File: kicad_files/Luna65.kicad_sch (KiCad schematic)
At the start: 384 parts, among them J1 Molex Power, J2 uC Pin Headers, J3 nRF51 Pin Headers, SW0 SW_Push, SW1 Mechanical_Switch, SW10 Mechanical_Switch, SW11 Mechanical_Switch, SW12 Mechanical_Switch, SW13 Mechanical_Switch, SW14 Mechanical_Switch, SW15 Mechanical_Switch, SW16 Mechanical_Switch, SW17 Mechanical_Switch, SW18 Mechanical_Switch, SW19 Mechanical_Switch, SW2 Mechanical_Switch, SW20 Mechanical_Switch, SW21 Mechanical_Switch, SW22 Mechanical_Switch, SW23 Mechanical_Switch, SW24 Mechanical_Switch, SW25 Mechanical_Switch, SW26 Mechanical_Switch, SW27 Mechanical_Switch, SW28 Mechanical_Switch, SW29 Mechanical_Switch, SW3 Mechanical_Switch, SW30 Mechanical_Switch, SW31 Mechanical_Switch, SW32 Mechanical_Switch, SW33 Mechanical_Switch, SW34 Mechanical_Switch, SW35 Mechanical_Switch, SW36 Mechanical_Switch, SW37 Mechanical_Switch, SW38 Mechanical_Switch, SW39 Mechanical_Switch, SW4 Mechanical_Switch, SW40 Mechanical_Switch, SW41 Mechanical_Switch, SW42 Mechanical_Switch, SW43 Mechanical_Switch, SW44 Mechanical_Switch, SW45 Mechanical_Switch, SW46 Mechanical_Switch, SW47 Mechanical_Switch, SW48 Mechanical_Switch, SW49 Mechanical_Switch, SW5 Mechanical_Switch, SW50 Mechanical_Switch, SW51 Mechanical_Switch, SW52 Mechanical_Switch, SW53 Mechanical_Switch, SW54 Mechanical_Switch, SW55 Mechanical_Switch, SW56 Mechanical_Switch, SW57 Mechanical_Switch, SW58 Mechanical_Switch, SW59 Mechanical_Switch, SW6 Mechanical_Switch, SW60 Mechanical_Switch, SW61 Mechanical_Switch, SW62 Mechanical_Switch, SW63 Mechanical_Switch, SW64 Mechanical_Switch, SW65 Mechanical_Switch, SW66 Mechanical_Switch, SW67 Mechanical_Switch, SW68 Mechanical_Switch, SW7 Mechanical_Switch, SW8 Mechanical_Switch, SW9 Mechanical_Switch, U1 ATMEGA32U4, U2 MBT40, U3 TXS0101DBVR, Y1 16MHz

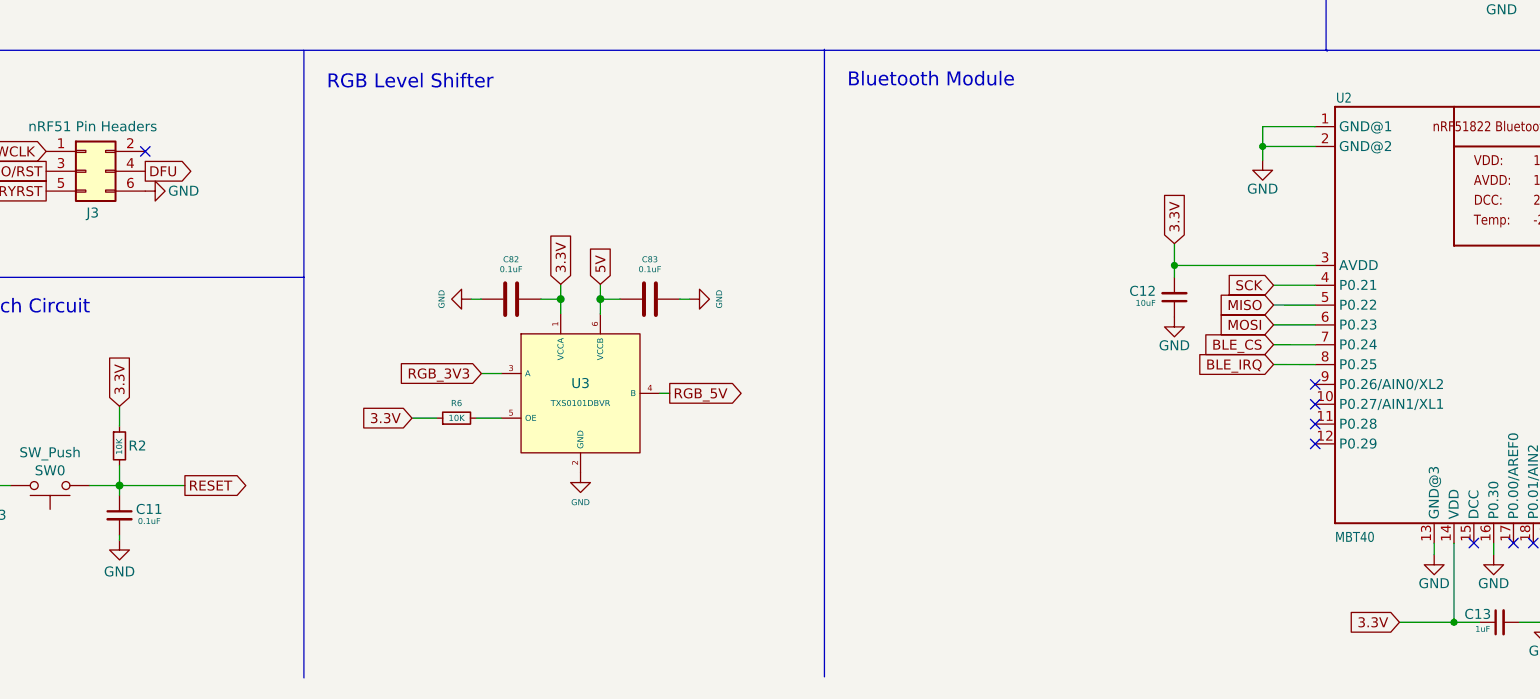
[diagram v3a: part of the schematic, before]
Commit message: Added 0 Ohm resistor to isolate BT and uC 3.3V
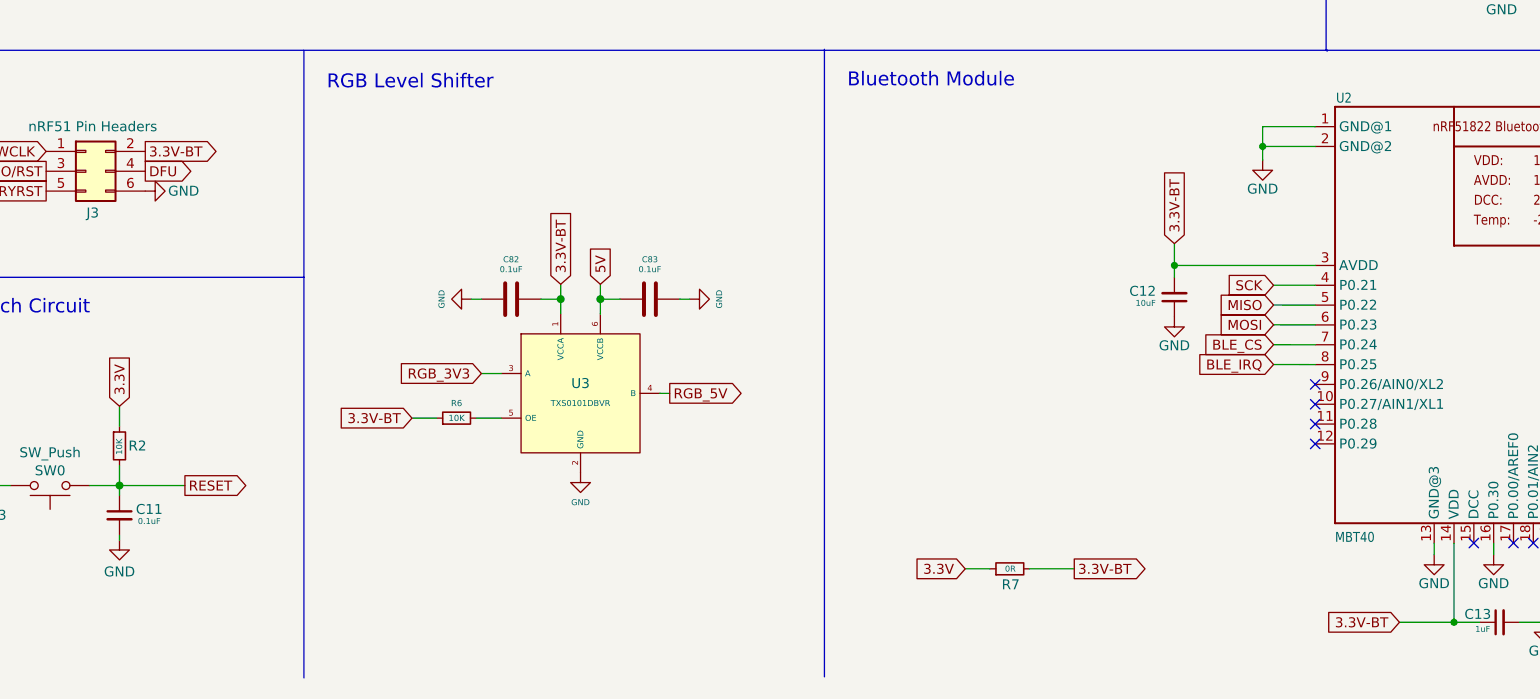
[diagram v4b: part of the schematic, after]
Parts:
- added R7: 0R, acheron_Components:R_SMD_1206, symbol Device:R_Small
- R6: footprint Resistor_SMD:R_0805_2012Metric_Pad1.20x1.40mm_HandSolder -> acheron_Components:C_0805_2012Metric
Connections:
- net 3.3V: now also R7.1; no longer C12.2, C13.1, C82.2, R6.1, U2.14 (VDD), U2.3 (AVDD), U3.1 (VCCA)
- net 3.3V-BT: now reaches J3.2 (Pin_2)
- net 3.3V-BT: now also C12.2, C13.1, C82.2, R6.1, U2.14 (VDD), U2.3 (AVDD), U3.1 (VCCA), R7.2
- no-connect marks 25 -> 24
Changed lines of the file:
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@@
   (no_connect (at 342.9 205.232))
   (no_connect (at 342.9 207.772))
-  (no_connect (at 132.08 185.547))
   (wire (pts (xy 262.636 151.892) (xy 262.636 150.368))
     (stroke (width 0) (type solid) (color 0 0 0 0))
@@
     (stroke (width 0) (type default) (color 0 0 0 0))
   )
+  (wire (pts (xy 245.364 239.014) (xy 251.079 239.014))
+    (stroke (width 0) (type default) (color 0 0 0 0))
+  )
   (wire (pts (xy 161.036 53.721) (xy 161.036 54.991))
     (stroke (width 0) (type solid) (color 0 0 0 0))
@@
     (stroke (width 0) (type default) (color 0 0 0 0))
   )
+  (wire (pts (xy 237.109 239.014) (xy 240.284 239.014))
+    (stroke (width 0) (type default) (color 0 0 0 0))
+  )
   (wire (pts (xy 479.171 217.805) (xy 483.616 217.805))
     (stroke (width 0) (type default) (color 0 0 0 0))
@@
     )
   )
+  (global_label "3.3V-BT" (shape output) (at 132.08 185.547 0) (fields_autoplaced)
+    (effects (font (size 1.27 1.27)) (justify left))
+    (property "Intersheet References" "${INTERSHEET_REFS}" (id 0) (at 142.606 185.4676 0)
+      (effects (font (size 1.27 1.27)) (justify left) hide)
+    )
+  )
   (global_label "5V" (shape input) (at 548.259 162.052 90)
     (effects (font (size 1.27 1.27)) (justify left))
@@
     )
   )
+  (global_label "3.3V" (shape input) (at 237.109 239.014 180) (fields_autoplaced)
+    (effects (font (size 1.27 1.27)) (justify right))
+    (property "Intersheet References" "${INTERSHEET_REFS}" (id 0) (at 230.393 239.0934 0)
+      (effects (font (size 1.27 1.27)) (justify right) hide)
+    )
+  )
   (global_label "5V" (shape input) (at 686.181 28.067 90)
     (effects (font (size 1.27 1.27)) (justify left))
@@
     )
   )
-  (global_label "3.3V" (shape input) (at 166.243 219.71 180)
+  (global_label "3.3V-BT" (shape input) (at 166.243 219.71 180)
     (effects (font (size 1.27 1.27)) (justify right))
     (property "Intersheet References" "${INTERSHEET_REFS}" (id 0) (at 107.823 -173.355 0)
@@
     )
   )
-  (global_label "3.3V" (shape input) (at 185.293 202.565 90)
+  (global_label "3.3V-BT" (shape input) (at 185.293 202.565 90)
     (effects (font (size 1.27 1.27)) (justify left))
     (property "Intersheet References" "${INTERSHEET_REFS}" (id 0) (at 116.078 -173.355 0)
@@
     )
   )
-  (global_label "3.3V" (shape input) (at 263.906 197.358 90) (fields_autoplaced)
+  (global_label "3.3V-BT" (shape input) (at 263.906 197.358 90) (fields_autoplaced)
     (effects (font (size 1.27 1.27)) (justify left))
-    (property "Intersheet References" "${INTERSHEET_REFS}" (id 0) (at 263.8266 190.642 90)
+    (property "Intersheet References" "${INTERSHEET_REFS}" (id 0) (at 263.8266 186.832 90)
       (effects (font (size 1.27 1.27)) (justify left) hide)
     )
@@
     )
   )
-  (global_label "3.3V" (shape input) (at 292.735 245.8624 180) (fields_autoplaced)
+  (global_label "3.3V-BT" (shape input) (at 292.735 245.8624 180) (fields_autoplaced)
     (effects (font (size 1.27 1.27)) (justify right))
-    (property "Intersheet References" "${INTERSHEET_REFS}" (id 0) (at 286.019 245.9418 0)
+    (property "Intersheet References" "${INTERSHEET_REFS}" (id 0) (at 282.209 245.783 0)
       (effects (font (size 1.27 1.27)) (justify right) hide)
     )
@@
     )
   )
+  (global_label "3.3V-BT" (shape output) (at 251.079 239.014 0) (fields_autoplaced)
+    (effects (font (size 1.27 1.27)) (justify left))
+    (property "Intersheet References" "${INTERSHEET_REFS}" (id 0) (at 261.605 238.9346 0)
+      (effects (font (size 1.27 1.27)) (justify left) hide)
+    )
+  )
   (global_label "SWCLK" (shape output) (at 345.059 197.612 0) (fields_autoplaced)
     (effects (font (size 1.27 1.27)) (justify left))
@@
     (pin "2")
   )
+  (symbol (lib_id "Device:R_Small") (at 242.824 239.014 90) (unit 1)
+    (in_bom yes) (on_board yes)
+    (property "Reference" "R7" (id 0) (at 244.094 241.046 90)
+      (effects (font (size 1.27 1.27)) (justify left))
+    )
+    (property "Value" "0R" (id 1) (at 243.586 239.014 90)
+      (effects (font (size 0.762 0.762)) (justify left))
+    )
+    (property "Footprint" "acheron_Components:R_SMD_1206" (id 2) (at 242.824 239.014 0)
+      (effects (font (size 1.27 1.27)) hide)
+    )
+    (property "Datasheet" "~" (id 3) (at 242.824 239.014 0)
+      (effects (font (size 1.27 1.27)) hide)
+    )
+    (pin "1")
+    (pin "2")
+  )
   (symbol (lib_id "Device:D_Small") (at 242.316 57.023 270) (unit 1)
     (in_bom yes) (on_board yes)
@@
       (effects (font (size 0.7874 0.7874)))
     )
-    (property "Footprint" "Resistor_SMD:R_0805_2012Metric_Pad1.20x1.40mm_HandSolder" (id 2) (at 171.958 219.71 0)
+    (property "Footprint" "acheron_Components:C_0805_2012Metric" (id 2) (at 171.958 219.71 0)
       (effects (font (size 1.27 1.27)) hide)
     )
@@
     )
     (path "/d0105023-a78a-4fde-ad78-42f8c2ce089d"
-      (reference "R6") (unit 1) (value "10K") (footprint "Resistor_SMD:R_0805_2012Metric_Pad1.20x1.40mm_HandSolder")
+      (reference "R6") (unit 1) (value "10K") (footprint "acheron_Components:C_0805_2012Metric")
+    )
+    (path "/7085f004-00f0-4a01-96a0-f17b9334734d"
+      (reference "R7") (unit 1) (value "0R") (footprint "acheron_Components:R_SMD_1206")
     )
     (path "/281baf33-ff67-42f7-9ce1-58f64fbc0df9"

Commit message: V7 Changes
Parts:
- removed C16, C17, C21, C22, C23, C24, C25, C26, C27, C28, C29, C30, C31, C32, C33, C34, C35, C36, C37, C38, C39, C40, C41, C42, C43, C44, C45, C46, C47, C48, C49, C50, C51, C52, C53, C54, C55, C56, C57, C58, C59, C60, C61, C62, C63, C64, C65, C66, C67, C68, C69, C70, C71, C72, C73, C74, C75, C76, C77, C78, C79, C80, C81: 0.1uF, acheron_Components:C_0805_2012Metric, symbol Device:C_Small
- removed D100, D101, D102, D103, D104, D105, D106, D107, D108, D109, D110, D111, D112, D113, D114, D115, D116, D117, D118, D119, D120, D121, D122, D123, D124, D125, D126, D127, D128, D129, D130, D131, D132, D133, D134, D135, D136, D71, D72, D73, D75, D76, D77, D78, D79, D80, D81, D82, D83, D84, D85, D86, D87, D88, D89, D90, D91, D92, D93, D94, D95, D96, D97, D98, D99: SK6812MINI-E, acheron_Components:SK6812MINI_3535_6028_3.2x2.8mm_Round, symbol acheron_Symbols:SK6812MINI-E
- removed D63: 1N4148W, acheron_Components:D_SOD-123, symbol Device:D_Small
- removed H1, H10, H11, H12, H2, H3, H4, H5, H6, H7, H8, H9: MountingHole, MountingHole:MountingHole_2.7mm_M2.5_Pad, symbol Mechanical:MountingHole
- removed J2: uC Pin Headers, Connector_PinHeader_2.54mm:PinHeader_2x03_P2.54mm_Vertical, symbol Connector_Generic:Conn_02x03_Odd_Even
- removed R7: 0R, acheron_Components:R_SMD_1206, symbol Device:R_Small
- removed SW63: Mechanical_Switch, acheron_MXH_metalrings:MX100H, symbol acheron_Symbols:Mechanical_Switch
- removed Y1: 16MHz, acheron_Components:Crystal_SMD_5032-2Pin, symbol Device:Crystal_Small
- added C19: 0.1uF, Capacitor_SMD:C_0603_1608Metric, symbol Device:C_Small
- added D100, D101, D102, D103, D104, D105, D106, D107, D108, D109, D110, D111, D112, D113, D114, D115, D116, D117, D118, D119, D120, D121, D122, D123, D124, D125, D126, D127, D128, D129, D130, D131, D132, D133, D134, D135, D136, D137, D71, D72, D73, D74, D75, D76, D77, D78, D79, D80, D81, D82, D83, D84, D85, D86, D87, D88, D89, D90, D91, D92, D93, D94, D95, D96, D97, D98, D99: LED, LED_SMD:LED_0805_2012Metric_Pad1.15x1.40mm_HandSolder, symbol Device:LED
- added D140, D141, D142: SK68XX_SIDE, Luna65:SK68XX_SIDE, symbol SK68XX_SIDE:SK68XX_SIDE
- added Q1: 2N7002, Package_TO_SOT_SMD:SOT-23, symbol Transistor_FET:2N7002
- added Q2: AO3401A, Package_TO_SOT_SMD:SOT-23, symbol Transistor_FET:AO3401A
- added R10, R13: 100, Resistor_SMD:R_0805_2012Metric_Pad1.20x1.40mm_HandSolder, symbol Device:R_Small
- added R11, R12: 10K, Resistor_SMD:R_0805_2012Metric_Pad1.20x1.40mm_HandSolder, symbol Device:R_Small
- added R14, R19: 1K, Resistor_SMD:R_0805_2012Metric_Pad1.20x1.40mm_HandSolder, symbol Device:R_Small
- added R82, R83, R9: 5.1R, Resistor_SMD:R_0603_1608Metric, symbol Device:R_Small
- added TP1, TP2: TestPoint, TestPoint:TestPoint_Pad_D2.0mm, symbol Connector:TestPoint
- added Y1: 16MHz, Crystal:Crystal_SMD_2520-4Pin_2.5x2.0mm, symbol Device:Crystal_GND24_Small
- C1: renamed from C9; footprint acheron_Components:C_0805_2012Metric -> Capacitor_SMD:C_0603_1608Metric
- C10: renamed from C11; footprint acheron_Components:C_0805_2012Metric -> Capacitor_SMD:C_0603_1608Metric
- C11: renamed from C12; value 10uF -> 1uF; footprint acheron_Components:C_0805_2012Metric -> Capacitor_SMD:C_0603_1608Metric
- C12: renamed from C13; footprint acheron_Components:C_0805_2012Metric -> Capacitor_SMD:C_0603_1608Metric
- C13: renamed from C19; footprint acheron_Components:C_0805_2012Metric -> Capacitor_SMD:C_0603_1608Metric
- C14, C15, C18, C20, C4, C5, C6, C7: footprint acheron_Components:C_0805_2012Metric -> Capacitor_SMD:C_0603_1608Metric
- C16: renamed from C82; footprint acheron_Components:C_0805_2012Metric -> Capacitor_SMD:C_0805_2012Metric_Pad1.18x1.45mm_HandSolder
- C17: renamed from C83; footprint acheron_Components:C_0805_2012Metric -> Capacitor_SMD:C_0805_2012Metric_Pad1.18x1.45mm_HandSolder
- C2: renamed from C10; footprint acheron_Components:C_0805_2012Metric -> Capacitor_SMD:C_0603_1608Metric
- C3: value 10uF -> 1uF; footprint acheron_Components:C_0805_2012Metric -> Capacitor_SMD:C_0603_1608Metric
- C8: renamed from C1; value 10uF -> 1uF; footprint acheron_Components:C_0805_2012Metric -> Capacitor_SMD:C_0603_1608Metric
- C9: renamed from C8; footprint acheron_Components:C_0805_2012Metric -> Capacitor_SMD:C_0603_1608Metric
- D70: MFN (none) -> Dongguan Opsco Optoelectronics; PKG (none) -> 3228
- J2: renamed from J3; footprint Connector_PinHeader_2.54mm:PinHeader_2x03_P2.54mm_Vertical -> Connector_PinHeader_1.27mm:PinHeader_2x05_P1.27mm_Vertical_SMD; symbol Connector_Generic:Conn_02x03_Odd_Even -> Connector_Generic:Conn_02x05_Odd_Even
- R1, R2, R3, R81: footprint acheron_Components:C_0805_2012Metric -> Resistor_SMD:R_0603_1608Metric
- R15, R16, R17, R18, R20, R21, R22, R23, R24, R25, R26, R27, R28, R29, R30, R31, R32, R33, R34, R35, R36, R37, R38, R39, R40, R41, R42, R43, R44, R45, R46, R47, R48, R49, R50, R51, R52, R53, R54, R55, R56, R57, R58, R59, R60, R61, R62, R63, R64, R65, R66, R67, R68, R69, R70, R71, R72, R73, R74, R75, R76, R77, R78, R79, R80: value 5.1R -> 1K; footprint acheron_Components:C_0805_2012Metric -> Resistor_SMD:R_0805_2012Metric_Pad1.20x1.40mm_HandSolder; Manufacturer (none) -> Uniroyal; Manufacturer Part Number (none) -> 0805W8F1001T5E; Package R0402 -> R0805; Specification (none) -> ±1% 125mW Thick Film Resistors 150V 0805; Vendor Part Number (none) -> LCSC C17513
- R4, R5: footprint acheron_Components:R_SMD_1206 -> Resistor_SMD:R_0805_2012Metric_Pad1.20x1.40mm_HandSolder
- R6: footprint acheron_Components:C_0805_2012Metric -> Resistor_SMD:R_0805_2012Metric_Pad1.20x1.40mm_HandSolder
- R7: renamed from R19; footprint acheron_Components:C_0805_2012Metric -> Resistor_SMD:R_0603_1608Metric
- R8: renamed from R14; footprint acheron_Components:C_0805_2012Metric -> Resistor_SMD:R_0603_1608Metric
- SW63: renamed from SW64; footprint acheron_MXH_metalrings:MX100H -> acheron_MXH_metalrings:MX125H
- SW64: renamed from SW65; footprint acheron_MXH_metalrings:MX100H -> acheron_MXH_metalrings:MX125H
- renumbered D137 to D138, D138 to D139, D68 to D63, D74 to D68, SW66 to SW65, SW67 to SW66, SW68 to SW67, SW0 to SW68
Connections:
- net 3.3V: now also C11.2, C12.1, C16.2, J2.1 (Pin_1), R6.1, U2.14 (VDD), U2.3 (AVDD), U3.1 (VCCA)
- net 5V: now also Q2.2 (S), R12.2, R82.2, R83.2, R9.2; no longer R15.2, R16.2, R17.2, R18.2, R20.2, R21.2, R22.2, R23.2, R24.2, R25.2, R26.2, R27.2, R28.2, R29.2, R30.2, R31.2, R32.2, R33.2, R34.2, R35.2, R36.2, R37.2, R38.2, R39.2, R40.2, R41.2, R42.2, R43.2, R44.2, R45.2, R46.2, R47.2, R48.2, R49.2, R50.2, R51.2, R52.2, R53.2, R54.2, R55.2, R56.2, R57.2, R58.2, R59.2, R60.2, R61.2, R62.2, R63.2, R64.2, R65.2, R66.2, R67.2, R68.2, R69.2, R70.2, R71.2, R72.2, R73.2, R74.2, R75.2, R76.2, R77.2, R78.2, R79.2, R80.2
- net Col1: now also U1.25 (ADC8/PD4); no longer U1.26 (ADC9/T1/PD6)
- net Col10: now also SW67.1; no longer SW58.1
- net Col11: now also SW66.1, U1.37 (ADC6/PF6); no longer SW67.1, U1.39 (ADC4/PF4)
- net Col12: now also SW57.1, U1.36 (ADC7/PF7); no longer SW66.1, U1.40 (ADC1/PF1)
- net Col2: now also U1.26 (ADC9/T1/PD6); no longer U1.27 (ADC10/T0/PD7)
- net Col3: now also U1.27 (ADC10/T0/PD7); no longer U1.28 (ADC4/PCINT11/PB4)
- net Col4: now also U1.28 (ADC4/PCINT11/PB4); no longer U1.29 (PCINT4/ADC12/PB5)
- net Col5: now also U1.29 (PCINT4/ADC12/PB5); no longer SW44.1, U1.30 (PCINT6/ADC13/PB6)
- net Col6: now also U1.30 (PCINT6/ADC13/PB6); no longer U1.31 (PC6)
- net Col7: now also U1.31 (PC6); no longer U1.32 (CLK/PC7)
- net Col8: now also U1.32 (CLK/PC7); no longer U1.36 (ADC7/PF7)
- net Col9: now also SW44.1, SW58.1, U1.39 (ADC4/PF4); no longer SW57.1, U1.37 (ADC6/PF6)
- net DFU: now also TP1.1; no longer J2.4 (Pin_4)
- net FCTRYRST: now also TP2.1; no longer J2.5 (Pin_5)
- net GND: now also J2.3 (Pin_3), J2.5 (Pin_5), C19.2, D100.1 (K), D101.1 (K), D102.1 (K), D103.1 (K), D104.1 (K), D105.1 (K), D106.1 (K), D107.1 (K), D108.1 (K), D109.1 (K), D110.1 (K), D111.1 (K), D112.1 (K), D113.1 (K), D114.1 (K), D115.1 (K), D116.1 (K), D117.1 (K), D118.1 (K), D119.1 (K), D120.1 (K), D121.1 (K), D122.1 (K), D123.1 (K), D124.1 (K), D125.1 (K), D126.1 (K), D127.1 (K), D128.1 (K), D129.1 (K), D130.1 (K), D131.1 (K), D132.1 (K), D133.1 (K), D134.1 (K), D135.1 (K), D136.1 (K), D137.1 (K), D140.4 (VSS), D141.4 (VSS), D142.4 (VSS), D71.1 (K), D72.1 (K), D73.1 (K), D74.1 (K), D75.1 (K), D76.1 (K), D77.1 (K), D78.1 (K), D79.1 (K), D80.1 (K), D81.1 (K), D82.1 (K), D83.1 (K), D84.1 (K), D85.1 (K), D86.1 (K), D87.1 (K), D88.1 (K), D89.1 (K), D90.1 (K), D91.1 (K), D92.1 (K), D93.1 (K), D94.1 (K), D95.1 (K), D96.1 (K), D97.1 (K), D98.1 (K), D99.1 (K), Q1.2 (S), R11.1, Y1.2, Y1.4; no longer J2.6 (Pin_6)
- net RGB_5V: now also D140.1 (DIN)
- net Row1: now also U1.19 (PD1/SDA/~{INT1}); no longer U1.18 (PD0/SCL/~{INT0})
- net Row2: now also U1.20 (PD2/RDX1/~{INT2}); no longer U1.19 (PD1/SDA/~{INT1})
- net Row3: now also U1.40 (ADC1/PF1); no longer U1.20 (PD2/RDX1/~{INT2})
- net Row4: now also U1.41 (ADC0/PF0); no longer U1.22 (PD5/~{CTS}/XCK1)
- net Row5: now also D44.1 (K)
- net Row6: now also U1.22 (PD5/~{CTS}/XCK1); no longer D44.1 (K), U1.41 (ADC0/PF0)
- net SWCLK: now also J2.4 (Pin_4); no longer J2.1 (Pin_1)
- net SWDIO/RST: now also J2.2 (Pin_2); no longer J2.3 (Pin_3), U1.25 (ADC8/PD4)
- net at C1.1, U1.16 (XTAL2): now also Y1.1
- net at C2.1, U1.17 (XTAL1): now also Y1.3
- net at R22.1: now also R15.1, R16.1, R17.1, R18.1, R20.1, R21.1, R23.1, R24.1, R25.1, R26.1, R27.1, R28.1, R29.2, R30.2, R31.2, R32.2, R33.2, R34.2, R35.2, R36.1, R37.1, R38.1, R39.1, R40.1, R41.1, R42.1, R43.1, R44.1, R45.1, R46.2, R47.2, R48.2, R49.2, R50.2, R51.1, R52.1, R53.1, R54.1, R55.1, R56.1, R57.1, R58.1, R59.1, R60.1, R61.1, R62.1, R63.1, R64.1, R65.1, R66.1, R67.1, R68.1, R69.2, R70.2, R71.2, R72.2, R73.1, R74.1, R75.1, R76.1, R77.1, R78.1, R79.1, R80.1, Q2.3 (D), R14.1, R19.1
- net at R33.1: now also D90.2 (A)
- net at R70.1: now also D127.2 (A)
- net at R34.1: now also D91.2 (A)
- net at R69.1: now also D126.2 (A)
- net at R32.1: now also D89.2 (A)
- net at R50.1: now also D107.2 (A)
- net at R71.1: now also D128.2 (A)
- net at D68.2 (DOUT): no longer D69.4 (DIN)
- net at D68.4 (DIN): now also D69.2 (DOUT)
- net RGB_NXT: now reaches D70.4 (DIN)
- net RGB_NXT: now also D142.3 (DOUT)
- net at R47.1: now also D104.2 (A)
- net at C18.1: now also R81.1, D140.2 (VDD); no longer R18.1
- net at R48.1: now also D105.2 (A)
- net at R35.1: now also D92.2 (A)
- net at R29.1: now also D86.2 (A)
- net at R46.1: now also D103.2 (A)
- net at R49.1: now also D106.2 (A)
- net at C15.1, D70.1 (VDD): now also R9.1; no longer R15.1
- net at R31.1: now also D88.2 (A)
- net at R30.1: now also D87.2 (A)
- net at R72.1: now also D129.2 (A)
- net at D70.2 (DOUT): now also D69.4 (DIN)
- net at C20.1: now also D142.2 (VDD), R83.1; no longer R20.1
- removed net 3.3V-BT: C11.2, C12.1, C16.2, J2.2 (Pin_2), R6.1, U2.14 (VDD), U2.3 (AVDD), U3.1 (VCCA)
- new net: D125.2 (A), R68.2
- new net: D85.2 (A), R28.2
- new net: Q2.1 (G), R13.1
- new net: D114.2 (A), R57.2
- new net: D112.2 (A), R55.2
- new net: D121.2 (A), R64.2
- new net: D84.2 (A), R27.2
- new net: D132.2 (A), R75.2
- new net: D78.2 (A), R21.2
- new net: D101.2 (A), R44.2
- new net: D131.2 (A), R74.2
- new net: D109.2 (A), R52.2
- new net: D100.2 (A), R43.2
- new net: D74.2 (A), R17.2
- new net: D75.2 (A), R18.2
- new net: D80.2 (A), R23.2
- new net: D98.2 (A), R41.2
- new net: C19.1, D141.2 (VDD), R82.1
- new net: D117.2 (A), R60.2
- new net: D113.2 (A), R56.2
- new net: D133.2 (A), R76.2
- new net: D77.2 (A), R20.2
- new net: Q1.1 (G), R10.2, R11.2
- new net: D102.2 (A), R45.2
- new net: D130.2 (A), R73.2
- new net: D123.2 (A), R66.2
- new net: D79.2 (A), R22.2
- new net: D99.2 (A), R42.2
- new net: D140.3 (DOUT), D141.1 (DIN)
- new net: D141.3 (DOUT), D142.1 (DIN)
- new net: Q1.3 (D), R12.1, R13.2
- new net: D108.2 (A), R51.2
- new net: D95.2 (A), R38.2
- new net: D122.2 (A), R65.2
- new net: D83.2 (A), R26.2
- new net: D76.2 (A), R19.2
- new net: D111.2 (A), R54.2
- new net: D120.2 (A), R63.2
- new net: D94.2 (A), R37.2
- new net: D71.2 (A), R14.2
- new net: D97.2 (A), R40.2
- new net: D115.2 (A), R58.2
- new net: D119.2 (A), R62.2
- new net: D93.2 (A), R36.2
- new net: D118.2 (A), R61.2
- new net: D134.2 (A), R77.2
- new net: D73.2 (A), R16.2
- new net: D96.2 (A), R39.2
- new net: D137.2 (A), R80.2
- new net: D136.2 (A), R79.2
- new net: D72.2 (A), R15.2
- new net: D110.2 (A), R53.2
- new net: D82.2 (A), R25.2
- new net: D124.2 (A), R67.2
- new net: D135.2 (A), R78.2
- new net: D116.2 (A), R59.2
- new net: D81.2 (A), R24.2
- new net BKLT: R10.1, U1.18 (PD0/SCL/~{INT0})
- no-connect marks 24 -> 29
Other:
- note added: "Decoupling capacitors"
- note added: "RGB Corner"
- note added: "RGB Side"
- note removed: "'"
- note removed: ","
- note removed: "-"
- note removed: "."
- note removed: "/"
- note removed: "0"
- note removed: "1"
- note removed: "2"
- note removed: "3"
- note removed: "4"
- note removed: "5"
- note removed: "6"
- note removed: "7"
- note removed: "8"
- note removed: "9"
- note removed: ":"
- note removed: "="
- note removed: "A"
- note removed: "B"
- note removed: "BKSP"
- note removed: "C"
- note removed: "CAPS"
- note removed: "D"
- note removed: "DOWN"
- note removed: "E"
- note removed: "END"
- note removed: "ENT"
- note removed: "ESC"
- note removed: "F"
- note removed: "FN"
- note removed: "G"
- note removed: "H"
- note removed: "HOME"
- note removed: "I"
- note removed: "J"
- note removed: "K"
- note removed: "L"
- note removed: "LALT"
- note removed: "LCTRL"
- note removed: "LEFT"
- note removed: "LSHFT"
- note removed: "M"
- note removed: "Mounting Holes"
- note removed: "N"
- note removed: "O"
- note removed: "P"
- note removed: "PGDN"
- note removed: "PGUP"
- note removed: "Q"
- note removed: "R"
- note removed: "RALT"
- note removed: "RCTRL"
- note removed: "RGB Matrix"
- note removed: "RIGHT"
- note removed: "RSHFT"
- note removed: "S"
- note removed: "SPACE"
- note removed: "T"
- note removed: "TAB"
- note removed: "U"
- note removed: "UP"
- note removed: "V"
- note removed: "W"
- note removed: "WIN"
- note removed: "X"
- note removed: "Y"
- note removed: "Z"
- note removed: "["
- note removed: "\"
- note removed: "]"
- moved on the sheet: C1, C10, C11, C12, C13, C14, C16, C17, C2, C3, C4, C5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
